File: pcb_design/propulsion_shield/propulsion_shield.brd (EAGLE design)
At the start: 100 x 56 mm, 62 parts

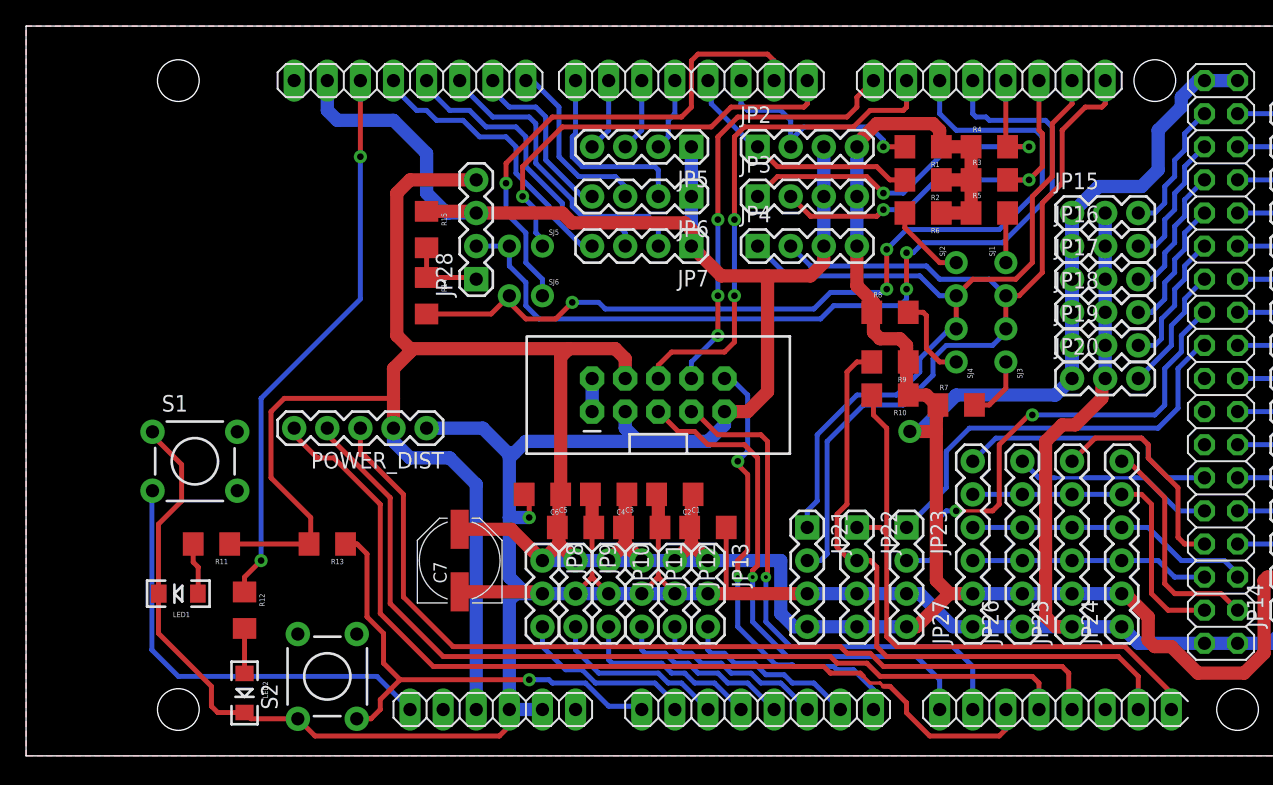
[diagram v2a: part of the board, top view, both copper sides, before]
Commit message: [propulsion_shield] Added Silkscreen on board
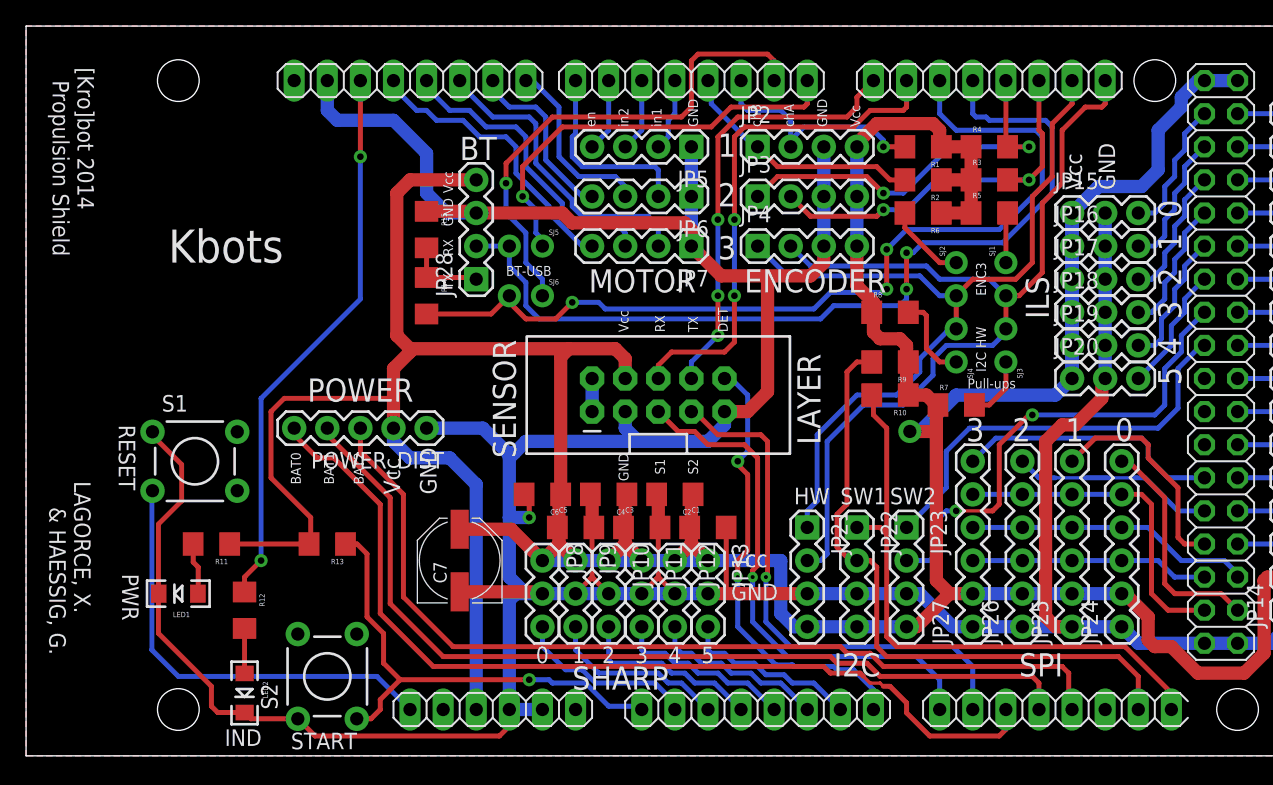
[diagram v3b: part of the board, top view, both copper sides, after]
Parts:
- R13: value 470 -> 10k
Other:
- board text added: "0"
- board text added: "1"
- board text added: "2"
- board text added: "3"
- board text added: "4"
- board text added: "5"
- board text added: "BAT0"
- board text added: "BAT1"
- board text added: "BAT2"
- board text added: "BT"
- board text added: "BT-USB"
- board text added: "DET"
- board text added: "ENC3"
- board text added: "ENCODER"
- board text added: "GND"
- board text added: "HW"
- board text added: "I2C"
- board text added: "I2C HW"
- board text added: "ILS"
- board text added: "IND"
- board text added: "Kbots"
- board text added: "LAGORCE, X. & HAESSIG, G."
- board text added: "LAYER"
- board text added: "MOTOR"
- board text added: "POWER"
- board text added: "PWR"
- board text added: "Pull-ups"
- board text added: "RESET"
- board text added: "RX"
- board text added: "S1"
- board text added: "S2"
- board text added: "SENSOR"
- board text added: "SHARP"
- board text added: "SPI"
- board text added: "START"
- board text added: "SW1"
- board text added: "SW2"
- board text added: "TX"
- board text added: "Vcc"
- board text added: "[Kro]bot 2014 Propulsion Shield"
- board text added: "chA"
- board text added: "chB"
- board text added: "en"
- board text added: "in1"
- board text added: "in2"
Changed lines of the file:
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@@
 <setting verticaltext="up"/>
 </settings>
-<grid distance="1" unitdist="mm" unit="mm" style="lines" multiple="1" display="yes" altdistance="0.005" altunitdist="inch" altunit="inch"/>
+<grid distance="0.01" unitdist="inch" unit="inch" style="lines" multiple="1" display="yes" altdistance="0.005" altunitdist="inch" altunit="inch"/>
 <layers>
 <layer number="1" name="Top" color="4" fill="1" visible="yes" active="yes"/>
@@
 <layer number="24" name="bOrigins" color="15" fill="1" visible="yes" active="yes"/>
 <layer number="25" name="tNames" color="7" fill="1" visible="yes" active="yes"/>
-<layer number="26" name="bNames" color="7" fill="1" visible="yes" active="yes"/>
+<layer number="26" name="bNames" color="7" fill="1" visible="no" active="yes"/>
 <layer number="27" name="tValues" color="7" fill="1" visible="no" active="yes"/>
 <layer number="28" name="bValues" color="7" fill="1" visible="no" active="yes"/>
@@
 <layer number="46" name="Milling" color="3" fill="1" visible="no" active="yes"/>
 <layer number="47" name="Measures" color="7" fill="1" visible="no" active="yes"/>
-<layer number="48" name="Document" color="7" fill="1" visible="yes" active="yes"/>
+<layer number="48" name="Document" color="7" fill="1" visible="no" active="yes"/>
 <layer number="49" name="Reference" color="7" fill="1" visible="no" active="yes"/>
 <layer number="50" name="dxf" color="7" fill="1" visible="no" active="no"/>
@@
 <dimension x1="0" y1="0" x2="0" y2="56" x3="-12" y3="28" textsize="1.778" textratio="15" layer="48"/>
 <dimension x1="0" y1="0" x2="100" y2="0" x3="50" y3="-6" textsize="1.778" textratio="15" layer="48"/>
+<text x="78.486" y="33.528" size="1.778" layer="21" font="vector" ratio="15" rot="R90">ILS</text>
+<text x="81.026" y="43.434" size="1.27" layer="21" font="vector" ratio="15" rot="R90">Vcc</text>
+<text x="83.566" y="43.434" size="1.27" layer="21" font="vector" ratio="15" rot="R90">GND</text>
+<text x="86.868" y="42.672" size="1.778" layer="21" font="vector" ratio="15" rot="R270">0</text>
+<text x="86.868" y="40.132" size="1.778" layer="21" font="vector" ratio="15" rot="R270">1</text>
+<text x="88.646" y="36.068" size="1.778" layer="21" font="vector" ratio="15" rot="R90">2</text>
+<text x="88.646" y="33.528" size="1.778" layer="21" font="vector" ratio="15" rot="R90">3</text>
+<text x="88.646" y="30.734" size="1.778" layer="21" font="vector" ratio="15" rot="R90">4</text>
+<text x="88.646" y="28.448" size="1.778" layer="21" font="vector" ratio="15" rot="R90">5</text>
+<text x="73.66" y="35.306" size="0.762" layer="21" font="vector" ratio="15" rot="R90">ENC3</text>
+<text x="73.66" y="29.464" size="0.762" layer="21" font="vector" ratio="15" rot="R90">I2C HW</text>
+<text x="75.946" y="28.956" size="0.762" layer="21" font="vector" ratio="15" rot="R180">Pull-ups</text>
+<text x="76.2" y="6.096" size="1.778" layer="21" font="vector" ratio="15">SPI</text>
+<text x="83.566" y="24.13" size="1.778" layer="21" font="vector" ratio="15">0</text>
+<text x="79.756" y="24.13" size="1.778" layer="21" font="vector" ratio="15">1</text>
+<text x="75.692" y="24.13" size="1.778" layer="21" font="vector" ratio="15">2</text>
+<text x="72.136" y="24.13" size="1.778" layer="21" font="vector" ratio="15">3</text>
+<text x="61.976" y="6.096" size="1.778" layer="21" font="vector" ratio="15">I2C</text>
+<text x="66.294" y="19.304" size="1.27" layer="21" font="vector" ratio="15">SW2</text>
+<text x="62.484" y="19.304" size="1.27" layer="21" font="vector" ratio="15">SW1</text>
+<text x="58.928" y="19.304" size="1.27" layer="21" font="vector" ratio="15">HW</text>
+<text x="41.91" y="5.08" size="1.778" layer="21" font="vector" ratio="15">SHARP</text>
+<text x="39.116" y="7.112" size="1.27" layer="21" font="vector" ratio="15">0</text>
+<text x="41.91" y="7.112" size="1.27" layer="21" font="vector" ratio="15">1</text>
+<text x="44.196" y="7.112" size="1.27" layer="21" font="vector" ratio="15">2</text>
+<text x="46.736" y="7.112" size="1.27" layer="21" font="vector" ratio="15">3</text>
+<text x="49.276" y="7.112" size="1.27" layer="21" font="vector" ratio="15">4</text>
+<text x="51.816" y="7.112" size="1.27" layer="21" font="vector" ratio="15">5</text>
+<text x="54.102" y="14.478" size="1.27" layer="21" font="vector" ratio="15">Vcc</text>
+<text x="54.102" y="11.938" size="1.27" layer="21" font="vector" ratio="15">GND</text>
+<text x="43.18" y="35.56" size="1.778" layer="21" font="vector" ratio="15">MOTOR</text>
+<text x="55.118" y="35.56" size="1.778" layer="21" font="vector" ratio="15">ENCODER</text>
+<text x="53.086" y="45.974" size="1.778" layer="21" font="vector" ratio="15">1</text>
+<text x="53.086" y="42.164" size="1.778" layer="21" font="vector" ratio="15">2</text>
+<text x="53.086" y="38.1" size="1.778" layer="21" font="vector" ratio="15">3</text>
+<text x="48.768" y="48.26" size="0.762" layer="21" font="vector" ratio="15" rot="R90">in1</text>
+<text x="46.228" y="48.26" size="0.762" layer="21" font="vector" ratio="15" rot="R90">in2</text>
+<text x="43.688" y="48.26" size="0.762" layer="21" font="vector" ratio="15" rot="R90">en</text>
+<text x="51.562" y="48.26" size="0.762" layer="21" font="vector" ratio="15" rot="R90">GND</text>
+<text x="64.008" y="48.26" size="0.762" layer="21" font="vector" ratio="15" rot="R90">Vcc</text>
+<text x="61.468" y="48.26" size="0.762" layer="21" font="vector" ratio="15" rot="R90">GND</text>
+<text x="58.928" y="48.26" size="0.762" layer="21" font="vector" ratio="15" rot="R90">chA</text>
+<text x="56.388" y="48.26" size="0.762" layer="21" font="vector" ratio="15" rot="R90">chB</text>
+<text x="36.83" y="36.83" size="0.762" layer="21" font="vector" ratio="15">BT-USB</text>
+<text x="33.274" y="45.72" size="1.778" layer="21" font="vector" ratio="15">BT</text>
+<text x="32.766" y="40.64" size="0.762" layer="21" font="vector" ratio="15" rot="R90">GND</text>
+<text x="32.766" y="43.18" size="0.762" layer="21" font="vector" ratio="15" rot="R90">Vcc</text>
+<text x="32.766" y="38.354" size="0.762" layer="21" font="vector" ratio="15" rot="R90">RX</text>
+<text x="32.766" y="35.814" size="0.762" layer="21" font="vector" ratio="15" rot="R90">TX</text>
+<text x="37.592" y="22.86" size="1.778" layer="21" font="vector" ratio="15" rot="R90">SENSOR</text>
+<text x="60.96" y="23.876" size="1.778" layer="21" font="vector" ratio="15" rot="R90">LAYER</text>
+<text x="21.59" y="27.178" size="1.778" layer="21" font="vector" ratio="15">POWER</text>
+<text x="31.496" y="20.066" size="1.27" layer="21" font="vector" ratio="15" rot="R90">GND</text>
+<text x="28.702" y="20.066" size="1.27" layer="21" font="vector" ratio="15" rot="R90">Vcc</text>
+<text x="25.908" y="20.828" size="0.762" layer="21" font="vector" ratio="15" rot="R90">BAT2</text>
+<text x="23.622" y="20.828" size="0.762" layer="21" font="vector" ratio="15" rot="R90">BAT1</text>
+<text x="21.082" y="20.828" size="0.762" layer="21" font="vector" ratio="15" rot="R90">BAT0</text>
+<text x="7.112" y="25.4" size="1.27" layer="21" font="vector" ratio="15" rot="SR270">RESET</text>
+<text x="7.366" y="13.97" size="1.27" layer="21" font="vector" ratio="15" rot="SR270">PWR</text>
+<text x="15.24" y="0.762" size="1.27" layer="21" font="vector" ratio="15" rot="SR0">IND</text>
+<text x="20.32" y="0.508" size="1.27" layer="21" font="vector" ratio="15" rot="SR0">START</text>
+<text x="1.778" y="21.082" size="1.27" layer="21" font="vector" ratio="15" rot="SR270">LAGORCE, X.
+    &amp; HAESSIG, G.</text>
+<text x="2.032" y="52.832" size="1.27" layer="21" font="vector" ratio="15" rot="SR270">[Kro]bot 2014
+  Propulsion Shield</text>
+<text x="10.922" y="37.846" size="2.54" layer="21" font="vector" ratio="15" rot="SR0">Kbots</text>
+<text x="46.228" y="32.512" size="0.762" layer="21" font="vector" ratio="15" rot="R90">Vcc</text>
+<text x="46.228" y="21.082" size="0.762" layer="21" font="vector" ratio="15" rot="R90">GND</text>
+<text x="49.022" y="32.512" size="0.762" layer="21" font="vector" ratio="15" rot="R90">RX</text>
+<text x="51.562" y="32.512" size="0.762" layer="21" font="vector" ratio="15" rot="R90">TX</text>
+<text x="53.848" y="32.512" size="0.762" layer="21" font="vector" ratio="15" rot="R90">DET</text>
+<text x="49.022" y="21.59" size="0.762" layer="21" font="vector" ratio="15" rot="R90">S1</text>
+<text x="51.562" y="21.59" size="0.762" layer="21" font="vector" ratio="15" rot="R90">S2</text>
 </plain>
 <attributes>
@@
 <element name="R11" library="SparkFun-Passives" package="1206" value="470" x="14.224" y="16.256" rot="R180"/>
 <element name="R12" library="SparkFun-Passives" package="1206" value="470" x="16.764" y="11.176" rot="R270"/>
-<element name="R13" library="SparkFun-Passives" package="1206" value="470" x="23.114" y="16.256" rot="R180"/>
+<element name="R13" library="SparkFun-Passives" package="1206" value="10k" x="23.114" y="16.256" rot="R180"/>
 <element name="R14" library="SparkFun-Passives" package="1206" value="1k" x="30.734" y="35.306" rot="R270"/>
 <element name="R15" library="SparkFun-Passives" package="1206" value="2k" x="30.734" y="40.386" rot="R270"/>
@@
 </board>
 </drawing>
+<compatibility>
+<note version="6.3" minversion="6.2.2" severity="warning">
+Since Version 6.2.2 text objects can contain more than one line,
+which will not be processed correctly with this version.
+</note>
+</compatibility>
 </eagle>
